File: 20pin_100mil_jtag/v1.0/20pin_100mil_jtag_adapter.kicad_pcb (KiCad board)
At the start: 2 copper layers, 14 x 27 mm, 50 parts, among them J1 Jumper, X1 JTAG-10, X2 JTAG-20

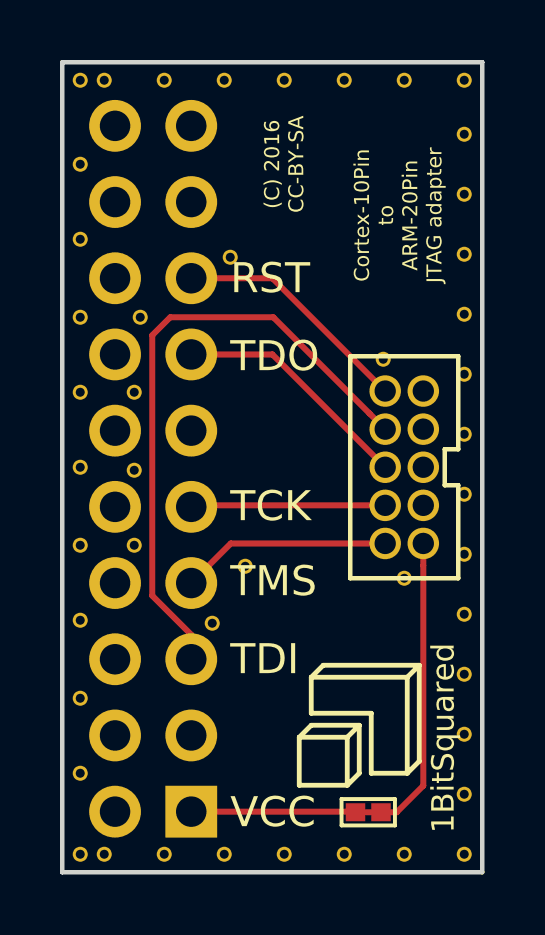
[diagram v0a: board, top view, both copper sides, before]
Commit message: Rounded 20pin adapter corners & minor cleanups.
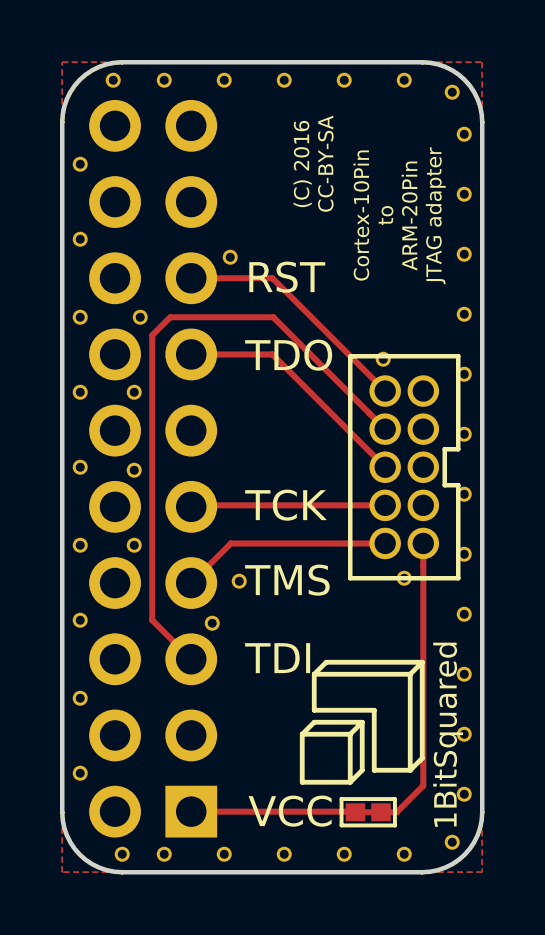
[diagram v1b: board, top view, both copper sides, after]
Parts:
- removed the REF** at (21.4, 46.4)
- removed the REF** at (21.4, 20.6)
- moved REF** 1.40 mm to (22.0, 46.4)
- moved REF** 1.10 mm to (21.7, 20.6)
- moved REF** 0.57 mm to (33.0, 21.0)
- moved REF** 0.57 mm to (33.0, 46.0)
- moved REF** 0.54 mm to (25.9, 37.3)
- moved REF** 0.14 mm to (30.0, 42.0)
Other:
- outline, holes or cut-outs redrawn
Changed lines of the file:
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@@
 (kicad_pcb (version 4) (host pcbnew 4.0.1-4.201602132031+6195~38~ubuntu14.04.1-stable)
   (general
-    (links 65)
+    (links 63)
     (no_connects 0)
     (area 19.924999 19.924999 34.075001 47.075001)
     (thickness 1.6)
-    (drawings 19)
-    (tracks 22)
+    (drawings 25)
+    (tracks 21)
     (zones 0)
-    (modules 50)
+    (modules 48)
     (nets 14)
   )
@@
   )
   (module pkl_misc:via0305 (layer F.Cu)
-    (at 26.1 36.8)
+    (at 25.9 37.3)
     (fp_text reference REF** (at 0 0.35) (layer F.SilkS) hide
       (effects (font (size 0.127 0.127) (thickness 0.03175)))
@@
   )
   (module pkl_misc:via0305 (layer F.Cu)
-    (at 21.4 46.4)
-    (fp_text reference REF** (at 0 0.35) (layer F.SilkS) hide
-      (effects (font (size 0.127 0.127) (thickness 0.03175)))
-    )
-    (fp_text value via0305 (at 0 -0.35) (layer F.Fab) hide
-      (effects (font (size 0.127 0.127) (thickness 0.03175)))
-    )
-    (pad "" thru_hole circle (at 0 0) (size 0.5 0.5) (drill 0.3) (layers *.Cu)
-      (net 1 GND) (zone_connect 2))
-  )
-  (module pkl_misc:via0305 (layer F.Cu)
     (at 23.4 46.4)
     (fp_text reference REF** (at 0 0.35) (layer F.SilkS) hide
@@
   )
   (module pkl_misc:via0305 (layer F.Cu)
-    (at 20.6 46.4)
+    (at 22 46.4)
     (fp_text reference REF** (at 0 0.35) (layer F.SilkS) hide
       (effects (font (size 0.127 0.127) (thickness 0.03175)))
@@
   )
   (module pkl_misc:via0305 (layer F.Cu)
-    (at 20.6 20.6)
-    (fp_text reference REF** (at 0 0.35) (layer F.SilkS) hide
-      (effects (font (size 0.127 0.127) (thickness 0.03175)))
-    )
-    (fp_text value via0305 (at 0 -0.35) (layer F.Fab) hide
-      (effects (font (size 0.127 0.127) (thickness 0.03175)))
-    )
-    (pad "" thru_hole circle (at 0 0) (size 0.5 0.5) (drill 0.3) (layers *.Cu)
-      (net 1 GND) (zone_connect 2))
-  )
-  (module pkl_misc:via0305 (layer F.Cu)
-    (at 21.4 20.6)
+    (at 21.7 20.6)
     (fp_text reference REF** (at 0 0.35) (layer F.SilkS) hide
       (effects (font (size 0.127 0.127) (thickness 0.03175)))
@@
   )
   (module pkl_misc:via0305 (layer F.Cu)
-    (at 33.4 20.6)
+    (at 33 21)
     (fp_text reference REF** (at 0 0.35) (layer F.SilkS) hide
       (effects (font (size 0.127 0.127) (thickness 0.03175)))
@@
       (rotate (xyz 0 0 180))
     )
+    (model walter/conn_strip/vasch_strip_10x2.wrl
+      (at (xyz 0.45 -0.05 -0.07000000000000001))
+      (scale (xyz 1 1 1))
+      (rotate (xyz 180 0 0))
+    )
   )
   (module pkl_samtec:FTSH-105-XX-X-D (layer F.Cu)
@@
     (pad 9 thru_hole circle (at 2.54 0.635 90) (size 1.05 1.05) (drill 0.71) (layers *.Cu *.Mask F.SilkS)
       (net 1 GND))
-    (model Pin_Headers.3dshapes/Pin_Header_Straight_2x05.wrl
+    (model walter/conn_strip/vasch_strip_5x2.wrl
       (at (xyz 0 0 0))
       (scale (xyz 0.5 0.5 0.5))
@@
   )
   (module pkl_misc:via0305 (layer F.Cu)
-    (at 33.4 46.4)
+    (at 33 46)
     (fp_text reference REF** (at 0 0.35) (layer F.SilkS) hide
       (effects (font (size 0.127 0.127) (thickness 0.03175)))
@@
   )
   (module pkl_logos:1b2_Logo_SilkS_4mm (layer F.Cu)
-    (at 29.9 42.1 90)
+    (at 30 42 90)
     (fp_text reference REF** (at 0 3 90) (layer F.Fab) hide
       (effects (font (size 1 1) (thickness 0.15)))
@@
       (net 9 /VCC))
   )
-  (gr_text "(C) 2016\nCC-BY-SA" (at 27.4 23.4 90) (layer F.SilkS)
+  (dimension 27 (width 0.3) (layer Dwgs.User)
+    (gr_text "27.000 mm" (at 37.35 33.5 270) (layer Dwgs.User)
+      (effects (font (size 1.5 1.5) (thickness 0.3)))
+    )
+    (feature1 (pts (xy 34 47) (xy 38.7 47)))
+    (feature2 (pts (xy 34 20) (xy 38.7 20)))
+    (crossbar (pts (xy 36 20) (xy 36 47)))
+    (arrow1a (pts (xy 36 47) (xy 35.413579 45.873496)))
+    (arrow1b (pts (xy 36 47) (xy 36.586421 45.873496)))
+    (arrow2a (pts (xy 36 20) (xy 35.413579 21.126504)))
+    (arrow2b (pts (xy 36 20) (xy 36.586421 21.126504)))
+  )
+  (dimension 14 (width 0.3) (layer Dwgs.User)
+    (gr_text "14.000 mm" (at 27 16.65) (layer Dwgs.User)
+      (effects (font (size 1.5 1.5) (thickness 0.3)))
+    )
+    (feature1 (pts (xy 34 20) (xy 34 15.3)))
+    (feature2 (pts (xy 20 20) (xy 20 15.3)))
+    (crossbar (pts (xy 20 18) (xy 34 18)))
+    (arrow1a (pts (xy 34 18) (xy 32.873496 18.586421)))
+    (arrow1b (pts (xy 34 18) (xy 32.873496 17.413579)))
+    (arrow2a (pts (xy 20 18) (xy 21.126504 18.586421)))
+    (arrow2b (pts (xy 20 18) (xy 21.126504 17.413579)))
+  )
+  (gr_arc (start 22 22) (end 20 22) (angle 90) (layer Edge.Cuts) (width 0.15))
+  (gr_arc (start 32 22) (end 32 20) (angle 90) (layer Edge.Cuts) (width 0.15))
+  (gr_arc (start 32 45) (end 34 45) (angle 90) (layer Edge.Cuts) (width 0.15))
+  (gr_arc (start 22 45) (end 22 47) (angle 90) (layer Edge.Cuts) (width 0.15))
+  (gr_text "(C) 2016\nCC-BY-SA" (at 28.4 23.4 90) (layer F.SilkS)
     (effects (font (size 0.5 0.5) (thickness 0.125)))
   )
-  (gr_text 1BitSquared (at 32.7 45.7 90) (layer F.SilkS)
+  (gr_text 1BitSquared (at 32.8 45.6 90) (layer F.SilkS)
     (effects (font (size 0.75 0.75) (thickness 0.1875)) (justify left))
   )
-  (gr_text RST (at 26 27.2 180) (layer B.SilkS)
+  (gr_text RST (at 26.1 27.2 180) (layer B.SilkS)
     (effects (font (size 1 1) (thickness 0.25)) (justify left mirror))
   )
-  (gr_text TDO (at 26 29.8 180) (layer B.SilkS)
+  (gr_text TDO (at 26.1 29.8 180) (layer B.SilkS)
     (effects (font (size 1 1) (thickness 0.25)) (justify left mirror))
   )
-  (gr_text TCK (at 26 34.8 180) (layer B.SilkS)
+  (gr_text TCK (at 26.1 34.8 180) (layer B.SilkS)
     (effects (font (size 1 1) (thickness 0.25)) (justify left mirror))
   )
-  (gr_text TMS (at 26 37.3 180) (layer B.SilkS)
+  (gr_text TMS (at 26.1 37.3 180) (layer B.SilkS)
     (effects (font (size 1 1) (thickness 0.25)) (justify left mirror))
   )
-  (gr_text TDI (at 26 39.9 180) (layer B.SilkS)
+  (gr_text TDI (at 26.2 39.9 180) (layer B.SilkS)
     (effects (font (size 1 1) (thickness 0.25)) (justify left mirror))
   )
-  (gr_text VCC (at 25.6 45) (layer F.SilkS)
+  (gr_text VCC (at 26.2 45) (layer F.SilkS)
     (effects (font (size 1 1) (thickness 0.25)) (justify left))
   )
@@
     (effects (font (size 0.5 0.5) (thickness 0.125)))
   )
-  (gr_text VCC (at 26 45 180) (layer B.SilkS)
+  (gr_text VCC (at 26.2 45 180) (layer B.SilkS)
     (effects (font (size 1 1) (thickness 0.25)) (justify left mirror))
   )
-  (gr_text TDI (at 25.6 39.9) (layer F.SilkS)
+  (gr_text TDI (at 26.1 39.9) (layer F.SilkS)
     (effects (font (size 1 1) (thickness 0.25)) (justify left))
   )
-  (gr_text TMS (at 25.6 37.3) (layer F.SilkS)
+  (gr_text TMS (at 26.1 37.3) (layer F.SilkS)
     (effects (font (size 1 1) (thickness 0.25)) (justify left))
   )
-  (gr_text TCK (at 25.6 34.8) (layer F.SilkS)
+  (gr_text TCK (at 26.1 34.8) (layer F.SilkS)
     (effects (font (size 1 1) (thickness 0.25)) (justify left))
   )
-  (gr_text TDO (at 25.6 29.8) (layer F.SilkS)
+  (gr_text TDO (at 26.1 29.8) (layer F.SilkS)
     (effects (font (size 1 1) (thickness 0.25)) (justify left))
   )
-  (gr_text RST (at 25.6 27.2) (layer F.SilkS)
+  (gr_text RST (at 26.1 27.2) (layer F.SilkS)
     (effects (font (size 1 1) (thickness 0.25)) (justify left))
   )
-  (gr_line (start 20 47) (end 20 20) (layer Edge.Cuts) (width 0.15))
-  (gr_line (start 34 47) (end 20 47) (layer Edge.Cuts) (width 0.15))
-  (gr_line (start 34 20) (end 34 47) (layer Edge.Cuts) (width 0.15))
-  (gr_line (start 20 20) (end 34 20) (layer Edge.Cuts) (width 0.15))
+  (gr_line (start 20 45) (end 20 22) (layer Edge.Cuts) (width 0.15))
+  (gr_line (start 32 47) (end 22 47) (layer Edge.Cuts) (width 0.15))
+  (gr_line (start 34 22) (end 34 45) (layer Edge.Cuts) (width 0.15))
+  (gr_line (start 22 20) (end 32 20) (layer Edge.Cuts) (width 0.15))
   (segment (start 30.765 36.04) (end 25.62 36.04) (width 0.2) (layer F.Cu) (net 8))
   (segment (start 25.62 36.04) (end 24.3 37.36) (width 0.2) (layer F.Cu) (net 8))
@@
   (segment (start 30.765 33.5) (end 27.005 29.74) (width 0.2) (layer F.Cu) (net 11))
   (segment (start 27.005 29.74) (end 24.3 29.74) (width 0.2) (layer F.Cu) (net 11))
-  (segment (start 24.3 39.9) (end 24.3 39.08213) (width 0.2) (layer F.Cu) (net 12))
-  (segment (start 24.3 39.08213) (end 23 37.78213) (width 0.2) (layer F.Cu) (net 12))
-  (segment (start 23 37.78213) (end 23 29.1) (width 0.2) (layer F.Cu) (net 12))
+  (segment (start 24.3 39.9) (end 23 38.6) (width 0.2) (layer F.Cu) (net 12))
+  (segment (start 30.240001 31.705001) (end 30.765 32.23) (width 0.2) (layer F.Cu) (net 12))
+  (segment (start 23 38.6) (end 23 29.1) (width 0.2) (layer F.Cu) (net 12))
   (segment (start 23 29.1) (end 23.6 28.5) (width 0.2) (layer F.Cu) (net 12))
+  (segment (start 23.6 28.5) (end 27.035 28.5) (width 0.2) (layer F.Cu) (net 12))
   (segment (start 27.035 28.5) (end 30.240001 31.705001) (width 0.2) (layer F.Cu) (net 12))
-  (segment (start 23.6 28.5) (end 27.035 28.5) (width 0.2) (layer F.Cu) (net 12))
-  (segment (start 30.240001 31.705001) (end 30.765 32.23) (width 0.2) (layer F.Cu) (net 12))
   (segment (start 30.765 30.96) (end 27.005 27.2) (width 0.2) (layer F.Cu) (net 13))
   (segment (start 27.005 27.2) (end 24.3 27.2) (width 0.2) (layer F.Cu) (net 13))
@@
     (polygon
       (pts
-        (xy 20 19.980421) (xy 34 19.980421) (xy 34 47) (xy 20 47)
+        (xy 20 20) (xy 34 20) (xy 34 47) (xy 20 47)
       )
     )

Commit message: Added reset button to the 20pin adapter.
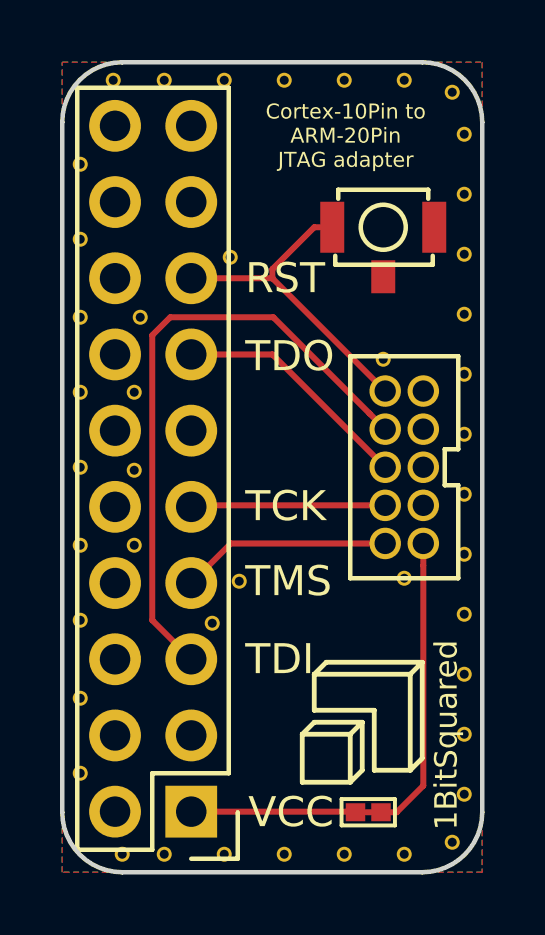
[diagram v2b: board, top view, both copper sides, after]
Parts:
- added SW1: TACT_G, pkl_buttons_switches:Tact_Switch_Top_GND_B3U-1100P, F.Cu at (30.7, 25.5)
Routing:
- net /RST: track 8.02 -> 10.9 mm
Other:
- board text added: "20pin adapter V1.0 (C) 2016 CC-BY-SA"
- board text removed: "(C) 2016 CC-BY-SA"
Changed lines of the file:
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@@
 (kicad_pcb (version 4) (host pcbnew 4.0.1-4.201602132031+6195~38~ubuntu14.04.1-stable)
   (general
-    (links 63)
-    (no_connects 0)
-    (area 19.924999 19.924999 34.075001 47.075001)
+    (links 66)
+    (no_connects 3)
+    (area 16.175 15.15 44 50.251191)
     (thickness 1.6)
-    (drawings 25)
-    (tracks 21)
+    (drawings 33)
+    (tracks 24)
     (zones 0)
-    (modules 48)
+    (modules 49)
     (nets 14)
   )
@@
     (zone_45_only no)
     (trace_min 0.2)
-    (segment_width 0.2)
+    (segment_width 0.15)
     (edge_width 0.15)
     (via_size 0.6)
@@
     (visible_elements FFFFFF7F)
     (pcbplotparams
-      (layerselection 0x00030_80000001)
-      (usegerberextensions false)
+      (layerselection 0x010f0_80000001)
+      (usegerberextensions true)
       (excludeedgelayer true)
       (linewidth 0.100000)
@@
       (outputformat 1)
       (mirror false)
-      (drillshape 1)
+      (drillshape 0)
       (scaleselection 1)
-      (outputdirectory ""))
+      (outputdirectory gerber))
   )
   (net 0 "")
@@
       (rotate (xyz 0 0 180))
     )
-    (model walter/conn_strip/vasch_strip_10x2.wrl
-      (at (xyz 0.45 -0.05 -0.07000000000000001))
-      (scale (xyz 1 1 1))
-      (rotate (xyz 180 0 0))
-    )
   )
   (module pkl_samtec:FTSH-105-XX-X-D (layer F.Cu)
@@
       (net 9 /VCC))
   )
+  (module pkl_buttons_switches:Tact_Switch_Top_GND_B3U-1100P (layer F.Cu)
+    (at 30.7 25.5)
+    (fp_text reference SW1 (at 0 3.5) (layer F.Fab)
+      (effects (font (size 1 1) (thickness 0.15)))
+    )
+    (fp_text value TACT_G (at 0 -2.5) (layer F.Fab)
+      (effects (font (size 1 1) (thickness 0.15)))
+    )
+    (fp_line (start -2.2 2.1) (end -2.2 -1.45) (layer F.CrtYd) (width 0.05))
+    (fp_line (start 2.2 2.1) (end -2.2 2.1) (layer F.CrtYd) (width 0.05))
+    (fp_line (start 2.2 -1.45) (end 2.2 2.1) (layer F.CrtYd) (width 0.05))
+    (fp_line (start -2.2 -1.45) (end 2.2 -1.45) (layer F.CrtYd) (width 0.05))
+    (fp_line (start 1.65 1.25) (end 1.65 0.95) (layer F.SilkS) (width 0.15))
+    (fp_line (start -1.6 1.25) (end -1.6 0.95) (layer F.SilkS) (width 0.15))
+    (fp_line (start 1.5 -1.25) (end 1.5 -0.95) (layer F.SilkS) (width 0.15))
+    (fp_line (start -1.5 -1.25) (end -1.5 -0.95) (layer F.SilkS) (width 0.15))
+    (fp_line (start -1.6 1.25) (end 1.65 1.25) (layer F.SilkS) (width 0.15))
+    (fp_line (start -1.5 -1.25) (end 1.5 -1.25) (layer F.SilkS) (width 0.15))
+    (fp_circle (center 0 0) (end 0.75 0) (layer F.SilkS) (width 0.15))
+    (pad 1 smd rect (at -1.7 0) (size 0.8 1.7) (layers F.Cu F.Paste F.Mask)
+      (net 13 /RST))
+    (pad 2 smd rect (at 1.7 0) (size 0.8 1.7) (layers F.Cu F.Paste F.Mask)
+      (net 1 GND))
+    (pad GND smd rect (at 0 1.65) (size 0.8 1.1) (layers F.Cu F.Paste F.Mask)
+      (net 1 GND))
+    (model esden/buttons/b3u_1100p.wrl
+      (at (xyz 0 0 0))
+      (scale (xyz 400 400 400))
+      (rotate (xyz 90 180 180))
+    )
+  )
+  (gr_line (start 20.5 46.25) (end 23 46.25) (layer F.SilkS) (width 0.15))
+  (gr_line (start 20.5 20.85) (end 20.5 46.25) (layer F.SilkS) (width 0.15))
+  (gr_line (start 25.55 20.85) (end 20.5 20.85) (layer F.SilkS) (width 0.15))
+  (gr_line (start 25.55 43.7) (end 25.55 20.85) (layer F.SilkS) (width 0.15))
+  (gr_line (start 23 43.7) (end 25.55 43.7) (layer F.SilkS) (width 0.15))
+  (gr_line (start 23 46.25) (end 23 43.7) (layer F.SilkS) (width 0.15))
+  (gr_line (start 25.85 46.55) (end 25.85 45) (layer F.SilkS) (width 0.15))
+  (gr_line (start 24.3 46.55) (end 25.85 46.55) (layer F.SilkS) (width 0.15))
   (dimension 27 (width 0.3) (layer Dwgs.User)
     (gr_text "27.000 mm" (at 37.35 33.5 270) (layer Dwgs.User)
@@
   (gr_arc (start 32 45) (end 34 45) (angle 90) (layer Edge.Cuts) (width 0.15))
   (gr_arc (start 22 45) (end 22 47) (angle 90) (layer Edge.Cuts) (width 0.15))
-  (gr_text "(C) 2016\nCC-BY-SA" (at 28.4 23.4 90) (layer F.SilkS)
-    (effects (font (size 0.5 0.5) (thickness 0.125)))
+  (gr_text "20pin adapter\nV1.0\n(C) 2016\nCC-BY-SA" (at 31.25 24.05 90) (layer B.SilkS)
+    (effects (font (size 0.5 0.5) (thickness 0.125)) (justify mirror))
   )
   (gr_text 1BitSquared (at 32.8 45.6 90) (layer F.SilkS)
@@
     (effects (font (size 1 1) (thickness 0.25)) (justify left))
   )
-  (gr_text "Cortex-10Pin\nto\nARM-20Pin\nJTAG adapter" (at 31.2 25.1 90) (layer F.SilkS)
+  (gr_text "Cortex-10Pin to\nARM-20Pin\nJTAG adapter" (at 29.45 22.45 360) (layer F.SilkS)
     (effects (font (size 0.5 0.5) (thickness 0.125)))
   )
@@
   (segment (start 23.6 28.5) (end 27.035 28.5) (width 0.2) (layer F.Cu) (net 12))
   (segment (start 27.035 28.5) (end 30.240001 31.705001) (width 0.2) (layer F.Cu) (net 12))
+  (segment (start 29 25.5) (end 28.4 25.5) (width 0.2) (layer F.Cu) (net 13))
+  (segment (start 28.4 25.5) (end 27.005 26.895) (width 0.2) (layer F.Cu) (net 13))
+  (segment (start 27.005 26.895) (end 27.005 27.2) (width 0.2) (layer F.Cu) (net 13))
   (segment (start 30.765 30.96) (end 27.005 27.2) (width 0.2) (layer F.Cu) (net 13))
   (segment (start 27.005 27.2) (end 24.3 27.2) (width 0.2) (layer F.Cu) (net 13))
